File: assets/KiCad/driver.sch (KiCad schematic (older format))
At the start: 33 parts

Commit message: minor update
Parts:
- removed Q? (x16): PN2222A, Package_TO_SOT_THT:TO-92_Inline, symbol Transistor_BJT:PN2222A
- removed R? (x16): 330, symbol Device:R
- removed U?: HD14514BP, symbol MyICs:HD14514BP

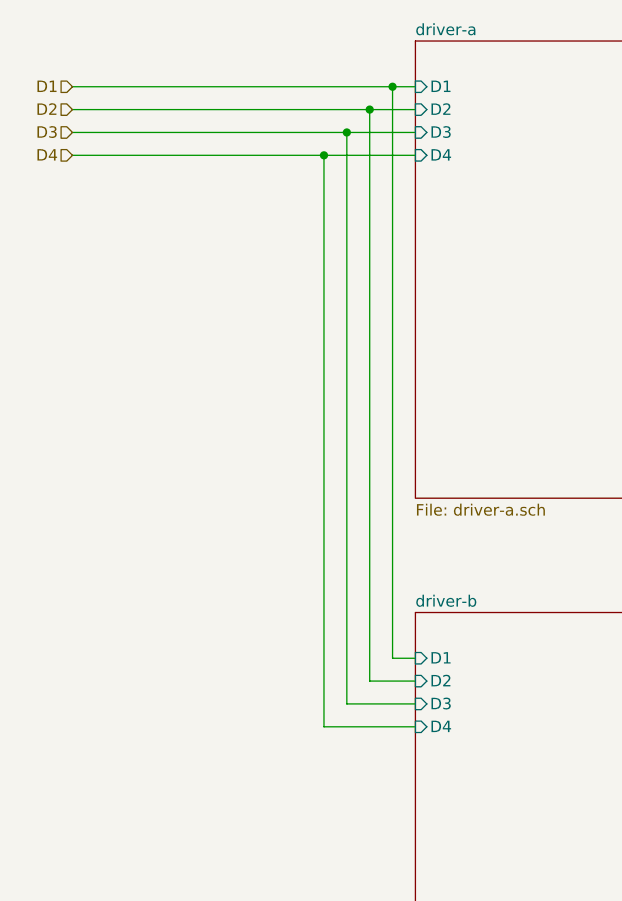
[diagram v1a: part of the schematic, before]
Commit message: update schematic
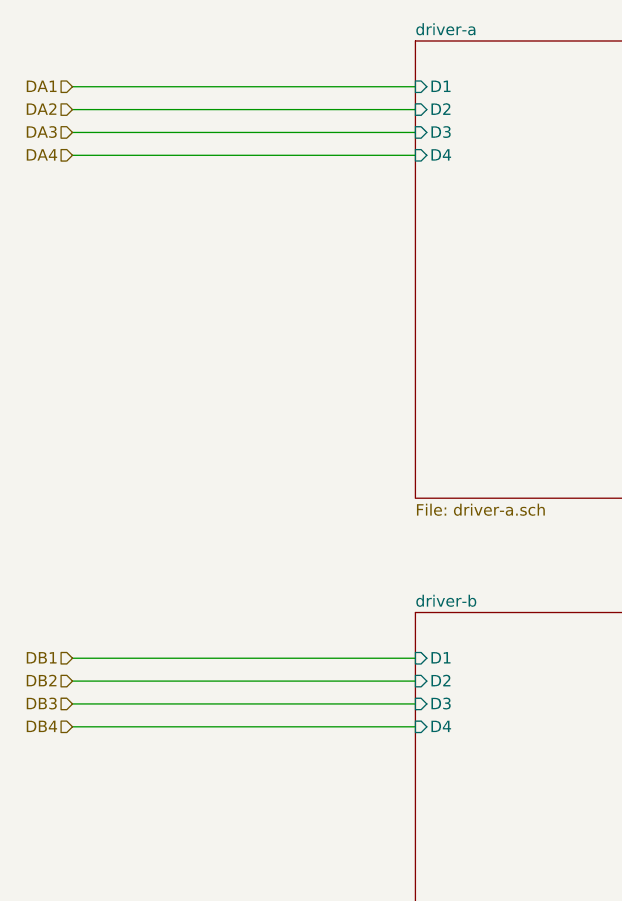
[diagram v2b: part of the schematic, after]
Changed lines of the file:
@@
 $Descr A4 11693 8268
 encoding utf-8
-Sheet 5 8
+Sheet 6 8
 Title ""
 Date ""
@@
 F21 "L15" O R 6500 5800 50
 $EndSheet
-Wire Wire Line
-	4500 1700 4400 1700
-Wire Wire Line
-	4500 1800 4300 1800
-Wire Wire Line
-	4500 1900 4200 1900
-Wire Wire Line
-	4500 2000 4100 2000
-Wire Wire Line
-	4500 4200 4400 4200
-Wire Wire Line
-	4400 4200 4400 1700
-Connection ~ 4400 1700
-Wire Wire Line
-	4400 1700 3000 1700
-Wire Wire Line
-	4500 4300 4300 4300
-Wire Wire Line
-	4300 4300 4300 1800
-Connection ~ 4300 1800
-Wire Wire Line
-	4300 1800 3000 1800
-Wire Wire Line
-	4500 4400 4200 4400
-Wire Wire Line
-	4200 4400 4200 1900
-Connection ~ 4200 1900
-Wire Wire Line
-	4200 1900 3000 1900
-Wire Wire Line
-	4500 4500 4100 4500
-Wire Wire Line
-	4100 4500 4100 2000
-Connection ~ 4100 2000
-Wire Wire Line
-	4100 2000 3000 2000
 Text HLabel 3000 1700 0    50   Input ~ 0
-D1
+DA1
 Text HLabel 3000 1800 0    50   Input ~ 0
-D2
+DA2
 Text HLabel 3000 1900 0    50   Input ~ 0
-D3
+DA3
 Text HLabel 3000 2000 0    50   Input ~ 0
-D4
+DA4
 Wire Wire Line
 	6500 1700 8000 1700
@@
 Text HLabel 8000 5800 2    50   Output ~ 0
 LB15
+Wire Wire Line
+	3000 2000 4500 2000
+Wire Wire Line
+	3000 1900 4500 1900
+Wire Wire Line
+	3000 1800 4500 1800
+Wire Wire Line
+	3000 1700 4500 1700
+Text HLabel 3000 4200 0    50   Input ~ 0
+DB1
+Text HLabel 3000 4300 0    50   Input ~ 0
+DB2
+Text HLabel 3000 4400 0    50   Input ~ 0
+DB3
+Text HLabel 3000 4500 0    50   Input ~ 0
+DB4
+Wire Wire Line
+	3000 4200 4500 4200
+Wire Wire Line
+	3000 4300 4500 4300
+Wire Wire Line
+	3000 4400 4500 4400
+Wire Wire Line
+	3000 4500 4500 4500
 $EndSCHEMATC

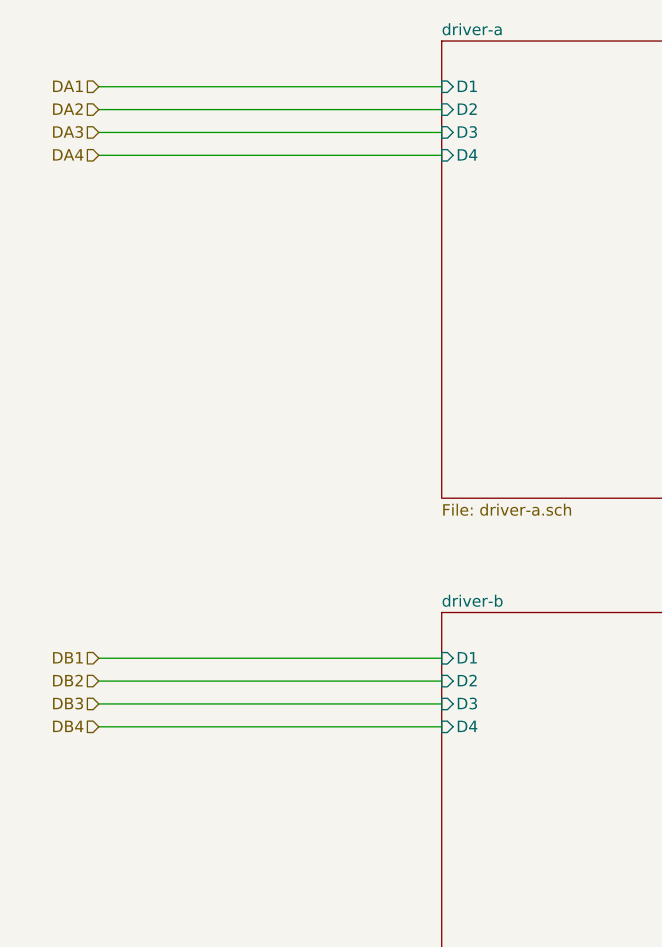
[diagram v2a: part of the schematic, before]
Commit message: schematic update
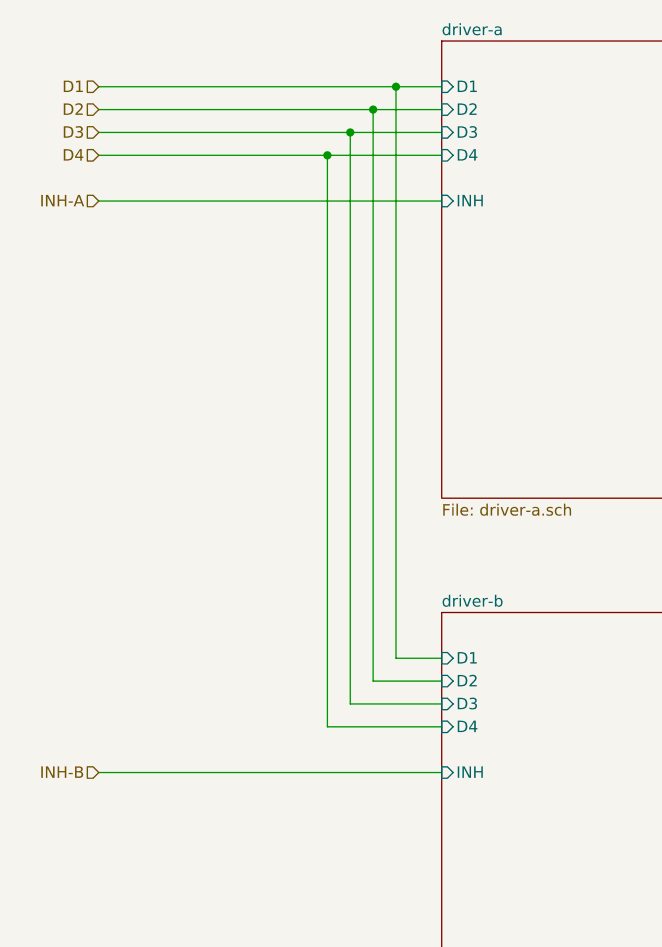
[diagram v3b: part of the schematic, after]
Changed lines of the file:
@@
 F20 "L14" O R 6500 3200 50
 F21 "L15" O R 6500 3300 50
+F22 "INH" I L 4500 2200 50
 $EndSheet
 $Sheet
@@
 F20 "L14" O R 6500 5700 50
 F21 "L15" O R 6500 5800 50
+F22 "INH" I L 4500 4700 50
 $EndSheet
 Text HLabel 3000 1700 0    50   Input ~ 0
-DA1
+D1
 Text HLabel 3000 1800 0    50   Input ~ 0
-DA2
+D2
 Text HLabel 3000 1900 0    50   Input ~ 0
-DA3
+D3
 Text HLabel 3000 2000 0    50   Input ~ 0
-DA4
+D4
 Wire Wire Line
 	6500 1700 8000 1700
@@
 LB15
 Wire Wire Line
-	3000 2000 4500 2000
-Wire Wire Line
-	3000 1900 4500 1900
-Wire Wire Line
-	3000 1800 4500 1800
-Wire Wire Line
-	3000 1700 4500 1700
-Text HLabel 3000 4200 0    50   Input ~ 0
-DB1
-Text HLabel 3000 4300 0    50   Input ~ 0
-DB2
-Text HLabel 3000 4400 0    50   Input ~ 0
-DB3
-Text HLabel 3000 4500 0    50   Input ~ 0
-DB4
-Wire Wire Line
-	3000 4200 4500 4200
-Wire Wire Line
-	3000 4300 4500 4300
-Wire Wire Line
-	3000 4400 4500 4400
-Wire Wire Line
-	3000 4500 4500 4500
+	3000 2000 4000 2000
+Wire Wire Line
+	3000 1900 4100 1900
+Wire Wire Line
+	3000 1800 4200 1800
+Wire Wire Line
+	3000 1700 4300 1700
+Wire Wire Line
+	4000 4500 4000 2000
+Wire Wire Line
+	4000 4500 4500 4500
+Connection ~ 4000 2000
+Wire Wire Line
+	4000 2000 4500 2000
+Wire Wire Line
+	4100 4400 4100 1900
+Wire Wire Line
+	4100 4400 4500 4400
+Connection ~ 4100 1900
+Wire Wire Line
+	4100 1900 4500 1900
+Wire Wire Line
+	4200 4300 4200 1800
+Wire Wire Line
+	4200 4300 4500 4300
+Connection ~ 4200 1800
+Wire Wire Line
+	4200 1800 4500 1800
+Wire Wire Line
+	4300 4200 4300 1700
+Wire Wire Line
+	4300 4200 4500 4200
+Connection ~ 4300 1700
+Wire Wire Line
+	4300 1700 4500 1700
+Text HLabel 3000 2200 0    50   Input ~ 0
+INH-A
+Text HLabel 3000 4700 0    50   Input ~ 0
+INH-B
+Wire Wire Line
+	3000 2200 4500 2200
+Wire Wire Line
+	3000 4700 4500 4700
 $EndSCHEMATC
